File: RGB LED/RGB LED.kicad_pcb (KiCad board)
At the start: 2 copper layers, 93.1 x 66.5 mm, 86 parts, among them J1 USB_C_Receptacle_USB2.0_16P, SW1 SW_SPST_FSMSM, SW2 SW_SPST_FSMSM, U1 AP2112K-3.3, U2 MAX7219, U3 ESP32-S3-WROOM-1-N4

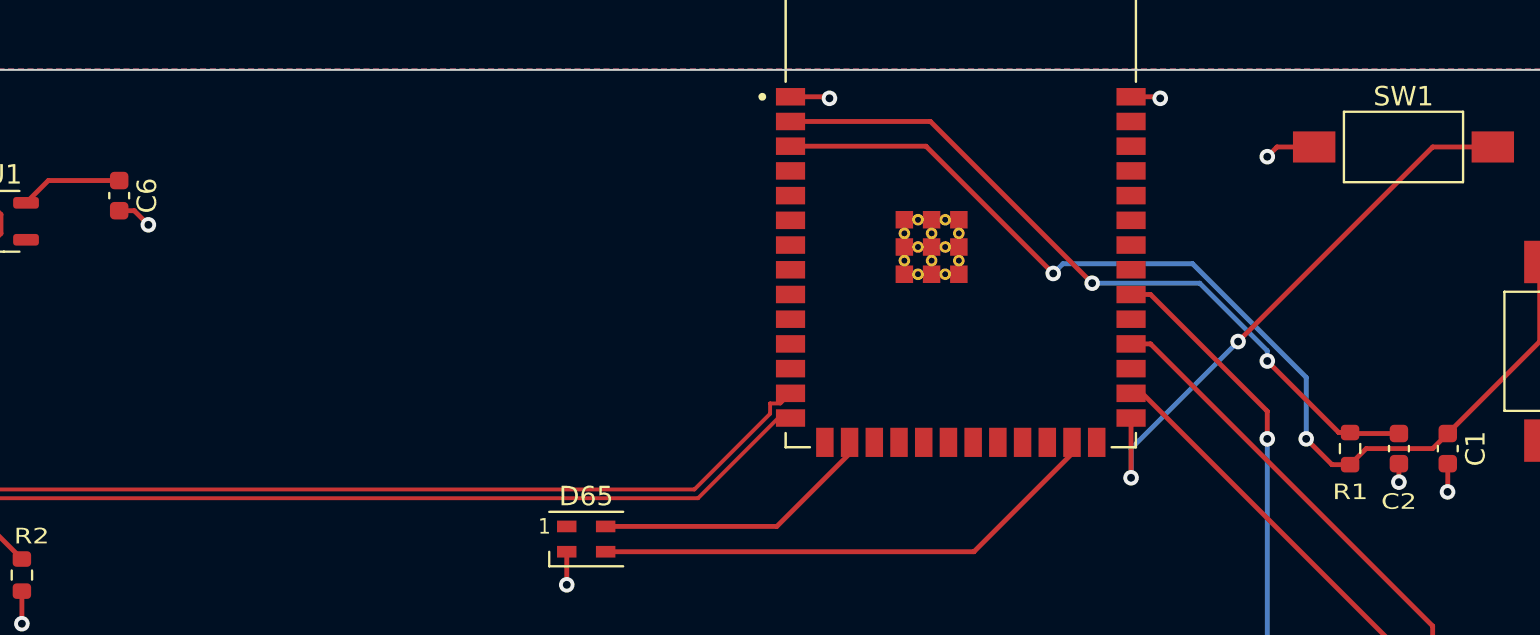
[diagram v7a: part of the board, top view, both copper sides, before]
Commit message: edited according to feedback
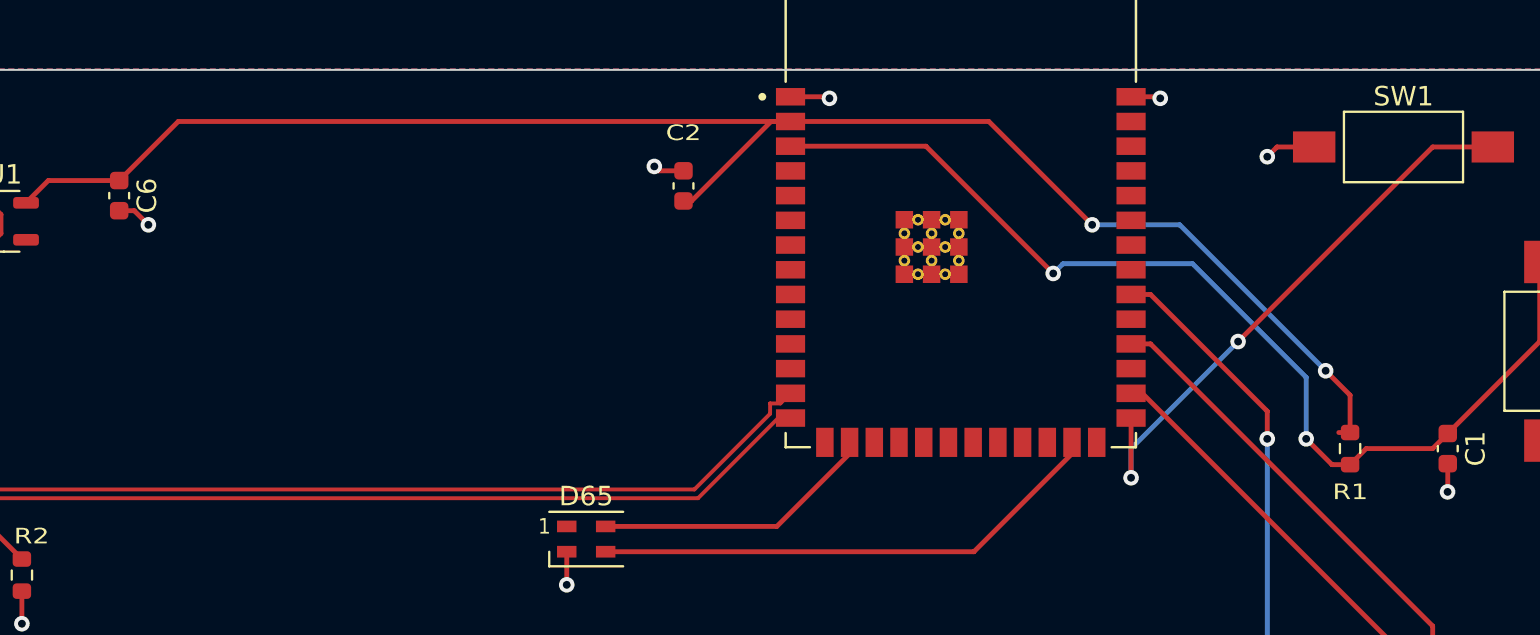
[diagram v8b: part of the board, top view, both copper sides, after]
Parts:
- moved C2 39.2 mm to (117.0, 47.0), turned to 90 degrees
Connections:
- C6 pad 1: +3V3 -> +3.3V
- U1 pad 5: +3V3 -> +3.3V
- U3 pad 41_10: GND -> (no net)
- U3 pad 41_11: GND -> (no net)
- U3 pad 41_12: GND -> (no net)
- U3 pad 41_13: GND -> (no net)
- U3 pad 41_14: GND -> (no net)
- U3 pad 41_15: GND -> (no net)
- U3 pad 41_16: GND -> (no net)
- U3 pad 41_17: GND -> (no net)
- U3 pad 41_18: GND -> (no net)
- U3 pad 41_19: GND -> (no net)
- U3 pad 41_20: GND -> (no net)
- U3 pad 41_21: GND -> (no net)
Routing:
- net +3.3V: track 38.2 -> 85.4 mm
- net +3V3: track 5.26 -> 0.00 mm
- net GND: track 27.0 -> 27.6 mm
